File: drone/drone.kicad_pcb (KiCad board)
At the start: 2 copper layers, 50.8 x 50.8 mm, 32 parts, among them J1 Conn_01x03, J2 Conn_02x03_Top_Bottom, J3 Conn_01x02, J4 Conn_01x02, J5 Conn_01x02, J6 Conn_01x02, Q1 Si2319CDS, Q2 Si2319CDS, Q3 Si2319CDS, Q4 Si2319CDS, U1 ATmega328P-A, U2 MPU-6050, U3 DWM1000, U4 BMP280

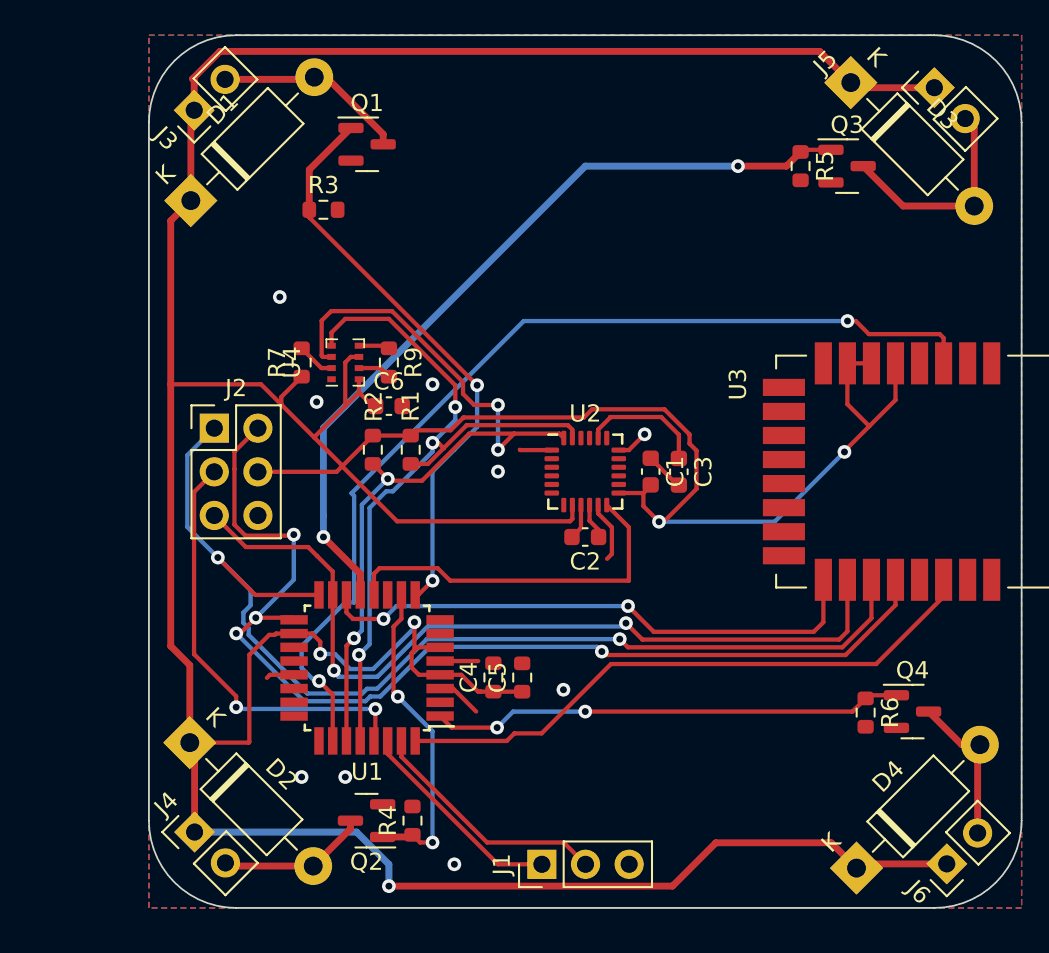
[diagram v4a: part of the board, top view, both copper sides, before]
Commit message: update pcb m328p to esp32
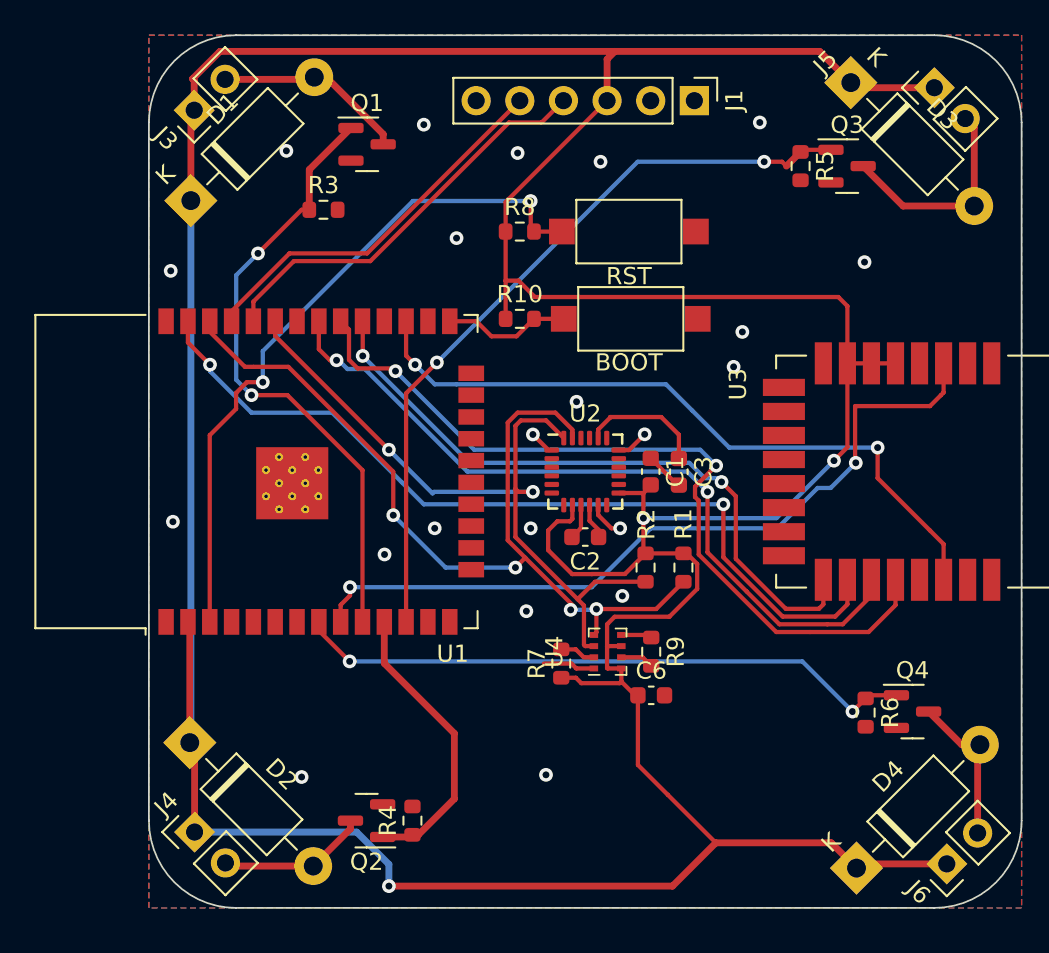
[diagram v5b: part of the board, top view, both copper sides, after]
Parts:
- removed C4, C5: C, Resistor_SMD:R_0603_1608Metric
- removed J2: Conn_02x03_Top_Bottom, Connector_PinHeader_2.54mm:PinHeader_2x03_P2.54mm_Vertical
- added BOOT: SW_Push_Open, Button_Switch_SMD:SW_SPST_CK_RS282G05A3, F.Cu at (104.2, 92.7)
- added R10: 10K, Resistor_SMD:R_0603_1608Metric, F.Cu at (97.8, 92.7)
- added R8: 10K, Resistor_SMD:R_0603_1608Metric, F.Cu at (97.8, 87.6)
- added RST: SW_Push_Open, Button_Switch_SMD:SW_SPST_CK_RS282G05A3, F.Cu at (104.1, 87.6)
- J1: value Conn_01x03 -> Conn_01x06; footprint Connector_PinHeader_2.54mm:PinHeader_1x03_P2.54mm_Vertical -> Connector_PinHeader_2.54mm:PinHeader_1x06_P2.54mm_Vertical
- U1: value ATmega328P-A -> ESP32-WROOM-32; footprint Package_QFP:TQFP-32_7x7mm_P0.8mm -> RF_Module:ESP32-WROOM-32
- moved J1 45.3 mm to (108.0, 80.0), turned to -90 degrees
- moved R7 23.1 mm to (100.2, 112.8)
- moved U4 22.7 mm to (102.9, 112.1)
- moved C6 22.7 mm to (105.4, 114.6)
- moved R9 22.7 mm to (105.4, 112.1)
- moved R1 17.3 mm to (107.3, 107.2)
- moved R2 17.3 mm to (105.1, 107.2)
- moved U1 11.9 mm to (85.5, 101.6), turned to 90 degrees
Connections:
- J1 pad 1: RX -> GND
- J1 pad 2: TX -> unconnected-(J1-Pad2)
- J1 pad 3: GND -> VCC
- U1 pad 1: MOTOR_4 -> GND
- U1 pad 10: MOTOR_2 -> MOTOR_1
- U1 pad 11: unconnected-(U1-Pad11) -> MOTOR_2
- U1 pad 12: MPU_IRQ -> MOTOR_3
- U1 pad 13: MOTOR_3 -> unconnected-(U1-Pad13)
- U1 pad 14: SS -> unconnected-(U1-Pad14)
- U1 pad 15: MOSI -> GND
- U1 pad 16: MISO -> unconnected-(U1-Pad16)
- U1 pad 17: SCK -> unconnected-(U1-Pad17)
- U1 pad 18: VCC -> unconnected-(U1-Pad18)
- U1 pad 2: unconnected-(U1-Pad2) -> VCC
- U1 pad 21: GND -> unconnected-(U1-Pad21)
- U1 pad 25: unconnected-(U1-Pad25) -> Net-(R10-Pad2)
- U1 pad 26: DW_RST -> unconnected-(U1-Pad26)
- U1 pad 27: SDA -> DW_IRQ
- U1 pad 28: SCL -> WS_IN
- U1 pad 29: RST -> SS
- U1 pad 3: GND -> Net-(R8-Pad2)
- U1 pad 30: RX -> SCK
- U1 pad 31: TX -> MISO
- U1 pad 32: DW_IRQ -> unconnected-(U1-Pad32)
- U1 pad 4: VCC -> unconnected-(U1-Pad4)
- U1 pad 5: GND -> unconnected-(U1-Pad5)
- U1 pad 6: VCC -> unconnected-(U1-Pad6)
- U1 pad 8: unconnected-(U1-Pad8) -> MOTOR_4
- U1 pad 9: MOTOR_1 -> DW_RST
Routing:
- net Net-(R8-Pad2): track 0.00 -> 40.3 mm, vias 0 -> 2
- net RST: track 25.2 -> 0.00 mm, vias 2 -> 0
- net ESP_RX: track 0.00 -> 24.0 mm
- net ESP_TX: track 0.00 -> 22.4 mm
- net MPU_IRQ: track 21.4 -> 0.00 mm
- net MISO: track 63.4 -> 44.1 mm
- net VCC: track 271.2 -> 254.3 mm, vias 5 -> 3
- net SCK: track 63.8 -> 47.6 mm, vias 4 -> 2
- net TX: track 14.2 -> 0.00 mm
- net RX: track 12.4 -> 0.00 mm
- net DW_RST: track 57.4 -> 45.2 mm
- net MOTOR_4: track 27.6 -> 36.5 mm
- net SCL: track 44.9 -> 52.6 mm, vias 3 -> 4
- net Net-(R10-Pad2): track 0.00 -> 7.42 mm
- net SS: track 32.6 -> 38.6 mm
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
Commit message: update hole
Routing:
- net GND: track 14.9 -> 17.0 mm
- net SDA: track 43.5 -> 42.8 mm
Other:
- outline, holes or cut-outs redrawn

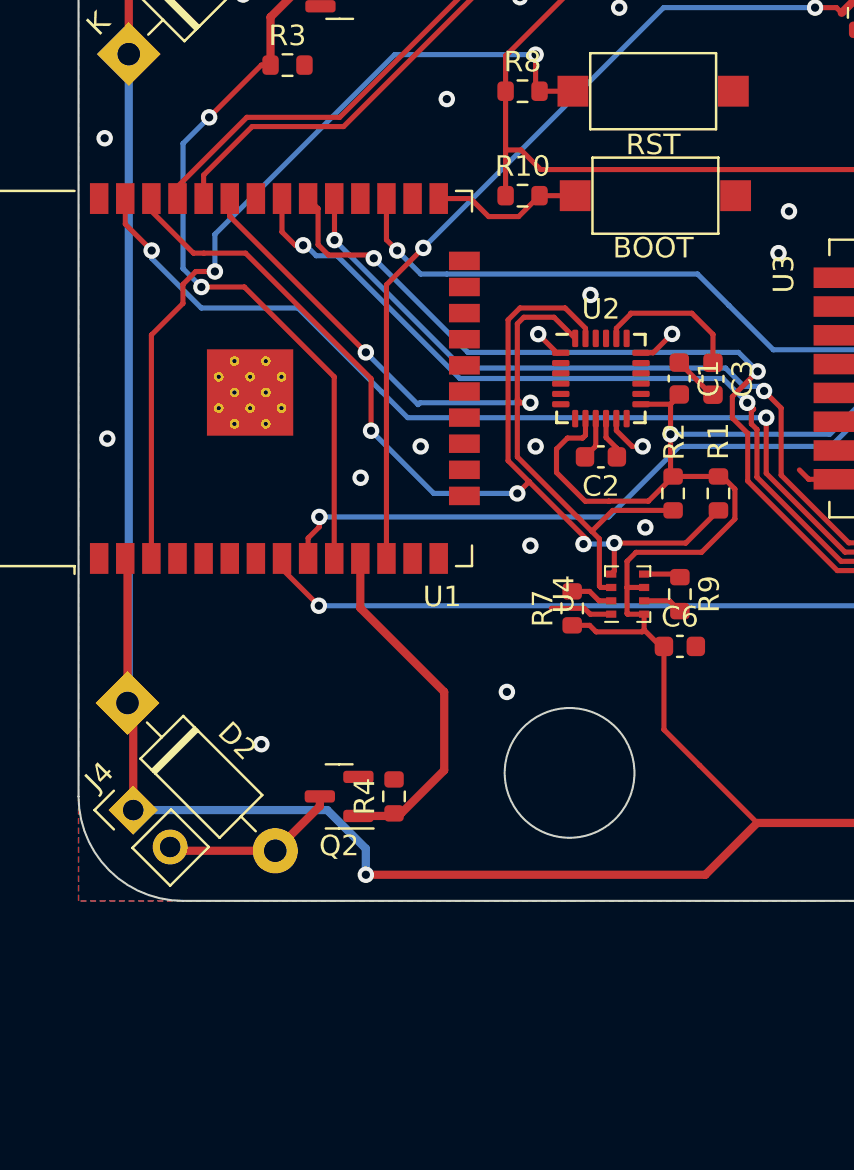
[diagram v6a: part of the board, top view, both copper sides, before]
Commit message: add tps63001
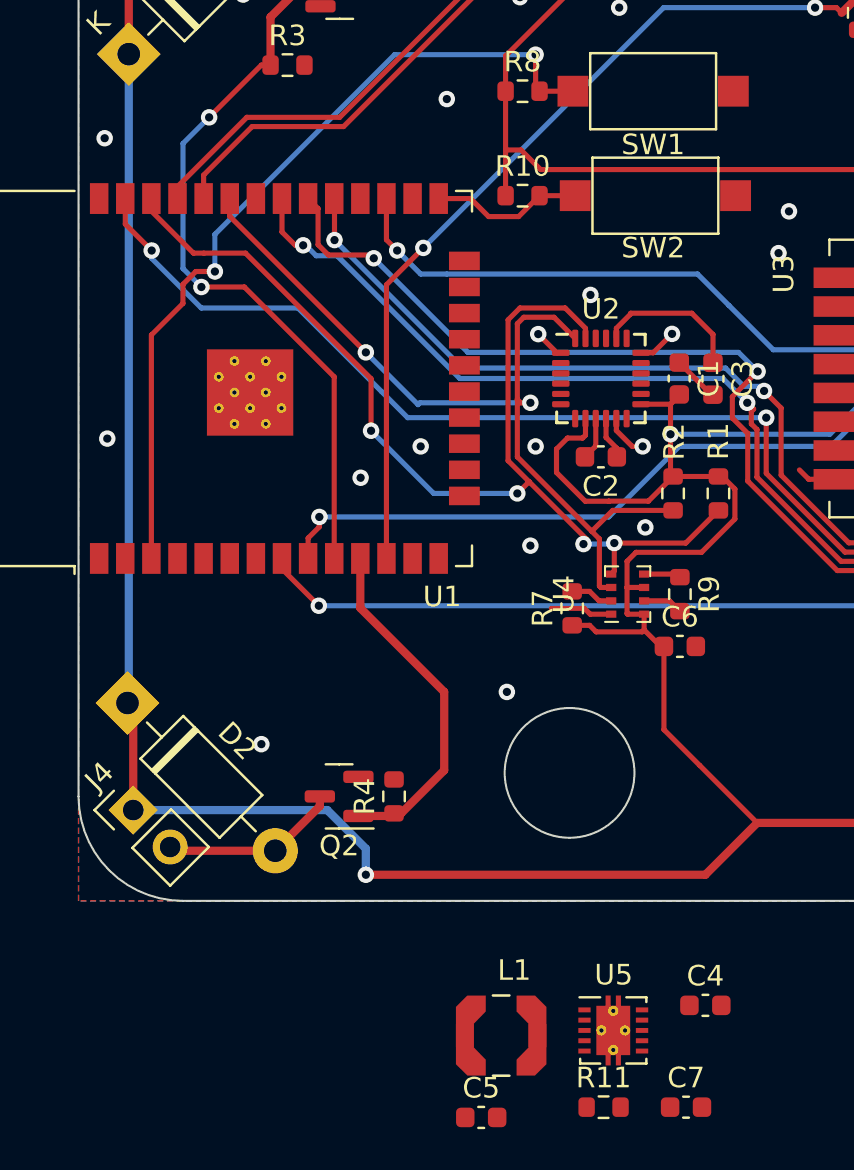
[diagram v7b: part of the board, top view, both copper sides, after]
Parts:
- added C4: 0.1uF, Capacitor_SMD:C_0603_1608Metric, F.Cu at (106.7, 132.1)
- added C5: 0.1uF, Capacitor_SMD:C_0603_1608Metric, F.Cu at (95.8, 137.5)
- added C7: 0.1uF, Capacitor_SMD:C_0603_1608Metric, F.Cu at (105.7, 137.0)
- added L1: LPS4012-103MRB, LPS4012:IND_LPS4012-103MRB, F.Cu at (96.8, 133.6)
- added R11: 100, Resistor_SMD:R_0603_1608Metric, F.Cu at (101.7, 137.0)
- added U5: TPS63001, Package_SON:Texas_DRC0010J_ThermalVias, F.Cu at (102.2, 133.3)
- renumbered RST to SW1, BOOT to SW2
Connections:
- D1 pad 1: VCC -> BAT+
- D2 pad 1: VCC -> BAT+
- D3 pad 1: VCC -> BAT+
- D4 pad 1: VCC -> BAT+
- J3 pad 1: VCC -> BAT+
- J4 pad 1: VCC -> BAT+
- J5 pad 1: VCC -> BAT+
- J6 pad 1: VCC -> BAT+
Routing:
- net VCC: track 254.3 -> 247.4 mm

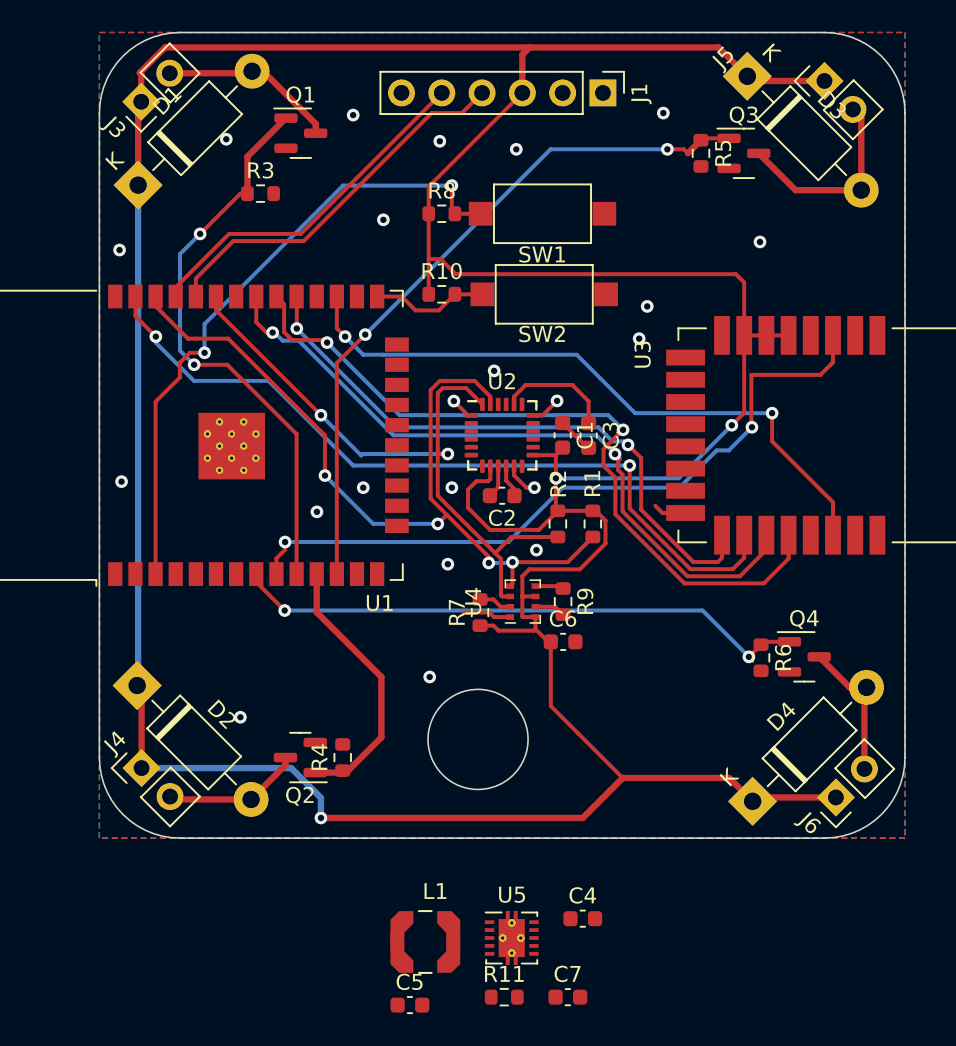
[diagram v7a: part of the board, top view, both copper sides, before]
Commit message: wiring tps63001
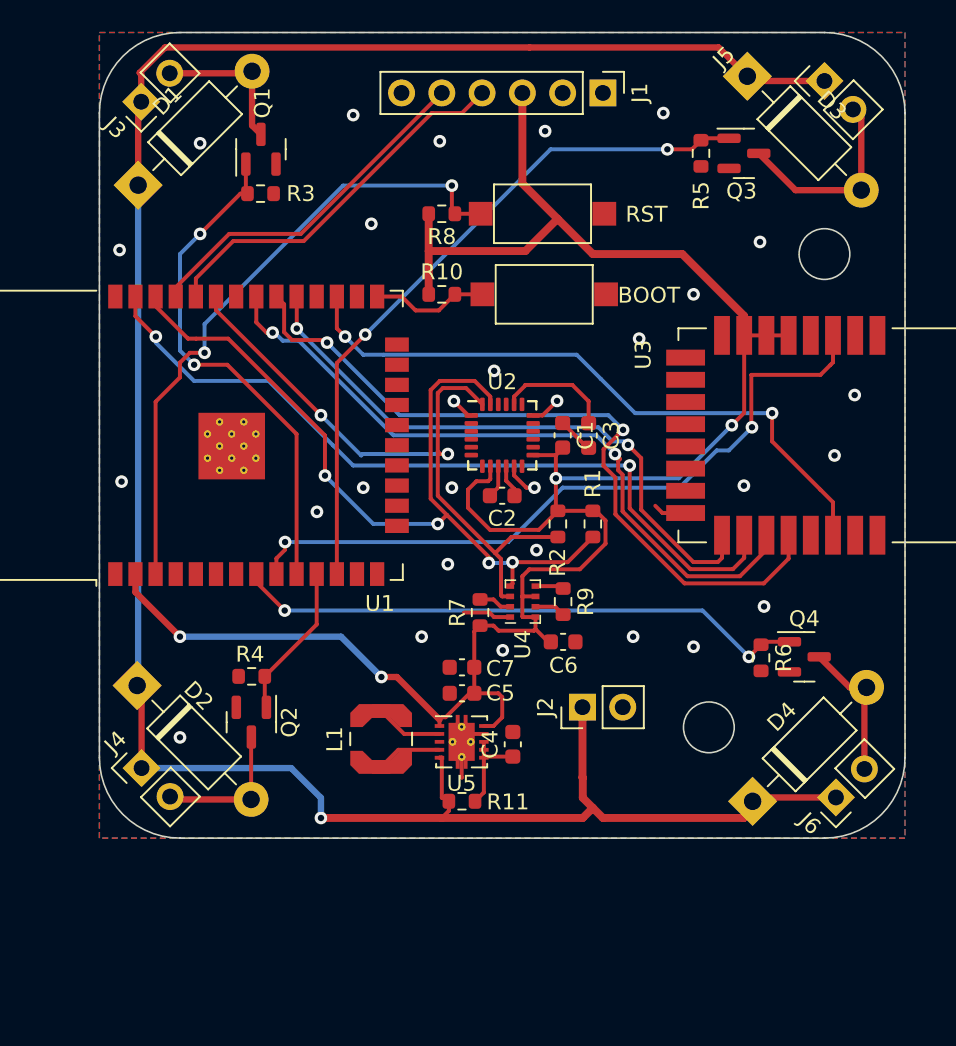
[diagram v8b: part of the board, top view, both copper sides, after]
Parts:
- added J2: Conn_01x02, Connector_PinHeader_2.54mm:PinHeader_1x02_P2.54mm_Vertical, F.Cu at (106.7, 118.7)
- moved C7 21.8 mm to (99.1, 116.2), turned to 180 degrees
- moved C5 19.9 mm to (99.1, 117.9), turned to 180 degrees
- moved L1 13.1 mm to (94.0, 120.7), turned to 90 degrees
- moved U5 12.8 mm to (99.0, 120.9)
- moved R11 12.6 mm to (99.1, 124.7)
- moved C4 11.8 mm to (102.3, 121.1), turned to 90 degrees
- moved R4 7.69 mm to (85.8, 116.8), turned to 180 degrees
- moved Q2 3.81 mm to (85.8, 119.7), turned to -90 degrees
- moved Q1 2.71 mm to (86.4, 83.6), turned to 90 degrees
- renumbered SW2 to BOOT, SW1 to RST
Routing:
- net BAT+: track 0.00 -> 147.1 mm, vias 0 -> 1
- net VCC: track 247.4 -> 132.7 mm, vias 3 -> 4
- net MOTOR_2: track 17.1 -> 9.80 mm
- net Net-(C4-Pad1): track 0.00 -> 5.83 mm
- net Net-(L1-Pad2): track 0.00 -> 4.28 mm
- net Net-(L1-Pad1): track 0.00 -> 4.13 mm
- net GND: track 17.0 -> 20.9 mm, vias 22 -> 29
- net MOTOR_1: track 36.0 -> 32.2 mm
- net Net-(D1-Pad2): track 11.2 -> 10.2 mm
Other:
- outline, holes or cut-outs redrawn
